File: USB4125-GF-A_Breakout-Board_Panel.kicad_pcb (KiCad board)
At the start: 2 copper layers, 81.3 x 76.2 mm, 140 parts, among them J1 Conn_01x04_Male, J2 Conn_01x03_Male, J3 USB4125-GF-A

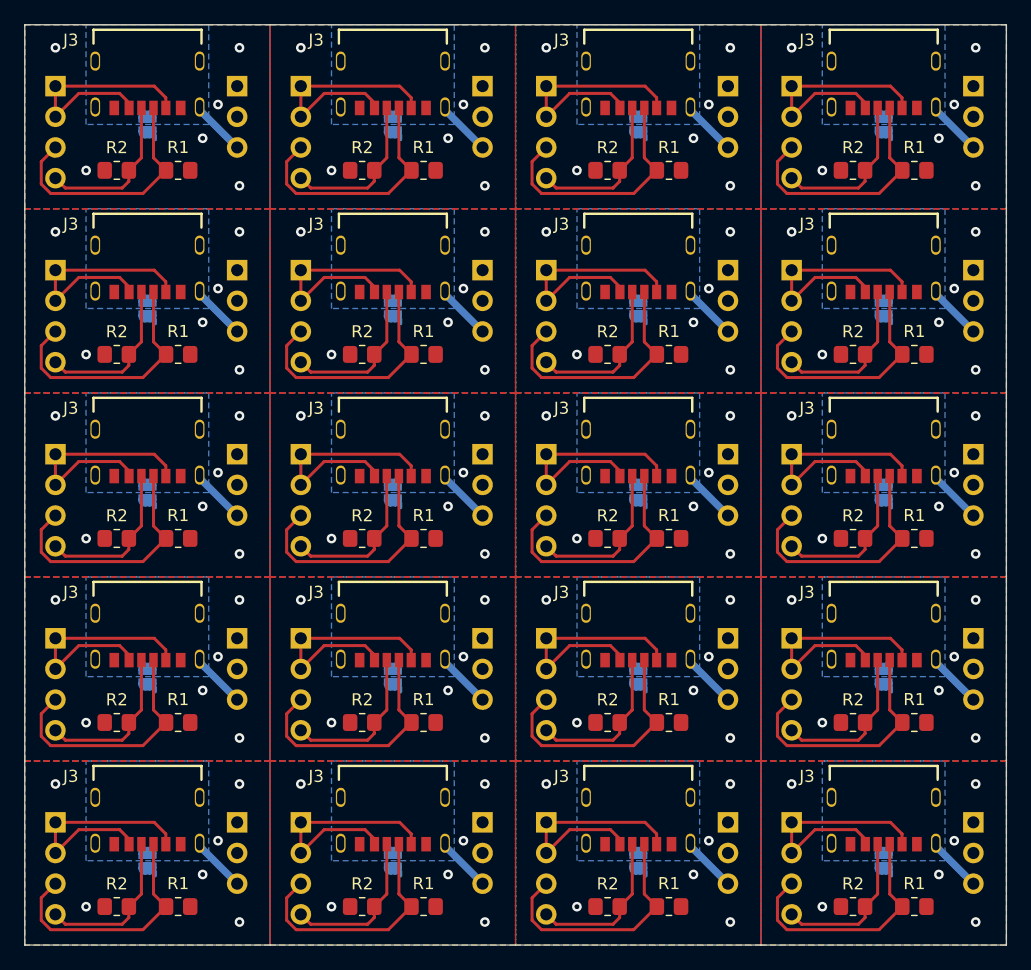
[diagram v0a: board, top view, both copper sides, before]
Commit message: Mod: Updated the project name and revision to be on the copper layer now
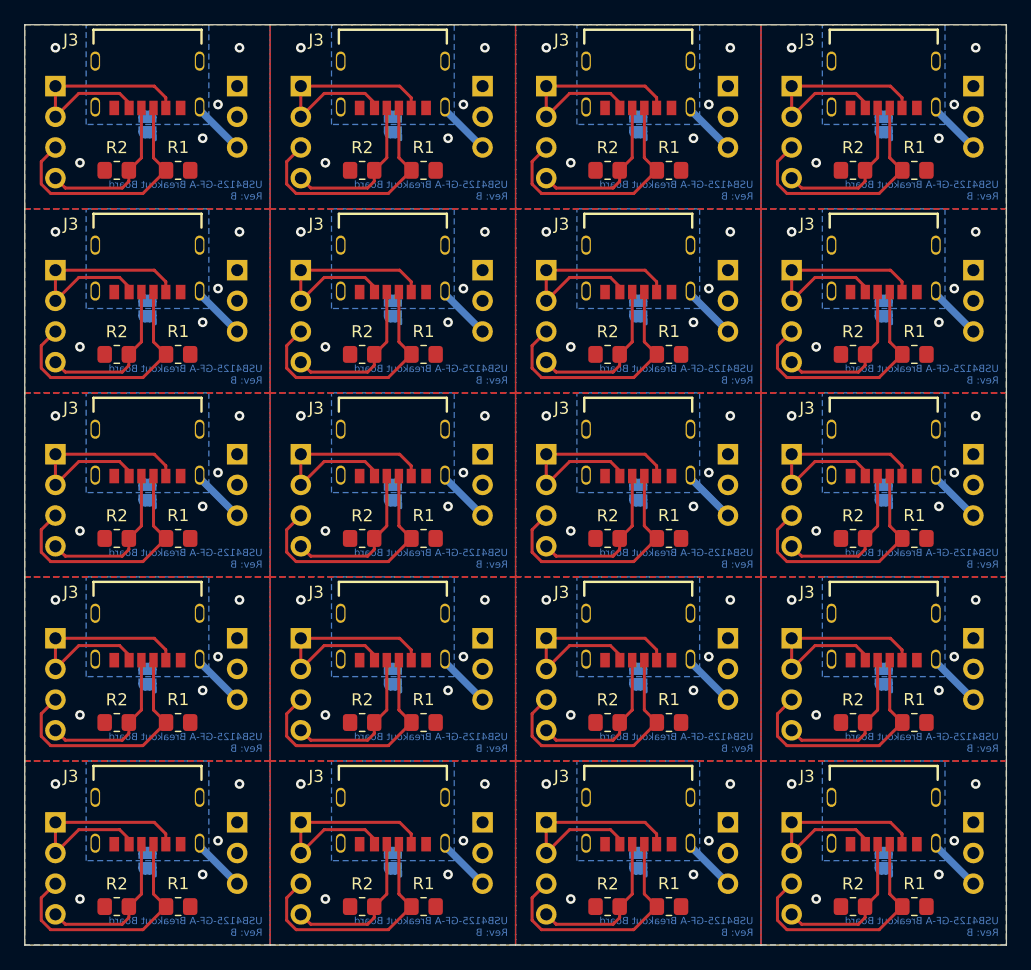
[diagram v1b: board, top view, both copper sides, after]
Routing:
- net Board_9-GND: vias 6 -> 5
- net Board_8-GND: vias 6 -> 5
- net Board_7-GND: vias 6 -> 5
- net Board_6-GND: vias 6 -> 5
- net Board_5-GND: vias 6 -> 5
- net Board_4-GND: vias 6 -> 5
- net Board_3-GND: vias 6 -> 5
- net Board_2-GND: vias 6 -> 5
- net Board_19-GND: vias 6 -> 5
- net Board_18-GND: vias 6 -> 5
- net Board_17-GND: vias 6 -> 5
- net Board_16-GND: vias 6 -> 5
- net Board_15-GND: vias 6 -> 5
- net Board_14-GND: vias 6 -> 5
- net Board_13-GND: vias 6 -> 5
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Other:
- board text added: "USB4125-GF-A Breakout Board Rev: B"
- board text removed: "Prj: USB4125-GF-A Breakout Board Rev: A"
